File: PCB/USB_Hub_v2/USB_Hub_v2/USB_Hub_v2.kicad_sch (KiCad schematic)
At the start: 74 parts, among them J1 USB_A, J2 USB_A, J3 USB_A, J4 USB_A, J5 USB_A, J6 USB_A, SW1 SW_Push_DPDT, U1 FE1.1s, U2 TS3USB30EDGSR, U3 TPS2116DRL, U4 USBLC6-2SC6, U5 USBLC6-2SC6, U6 USBLC6-2SC6, U7 USBLC6-2SC6, U8 USBLC6-2SC6, U9 USBLC6-2SC6, Y1 12MHz

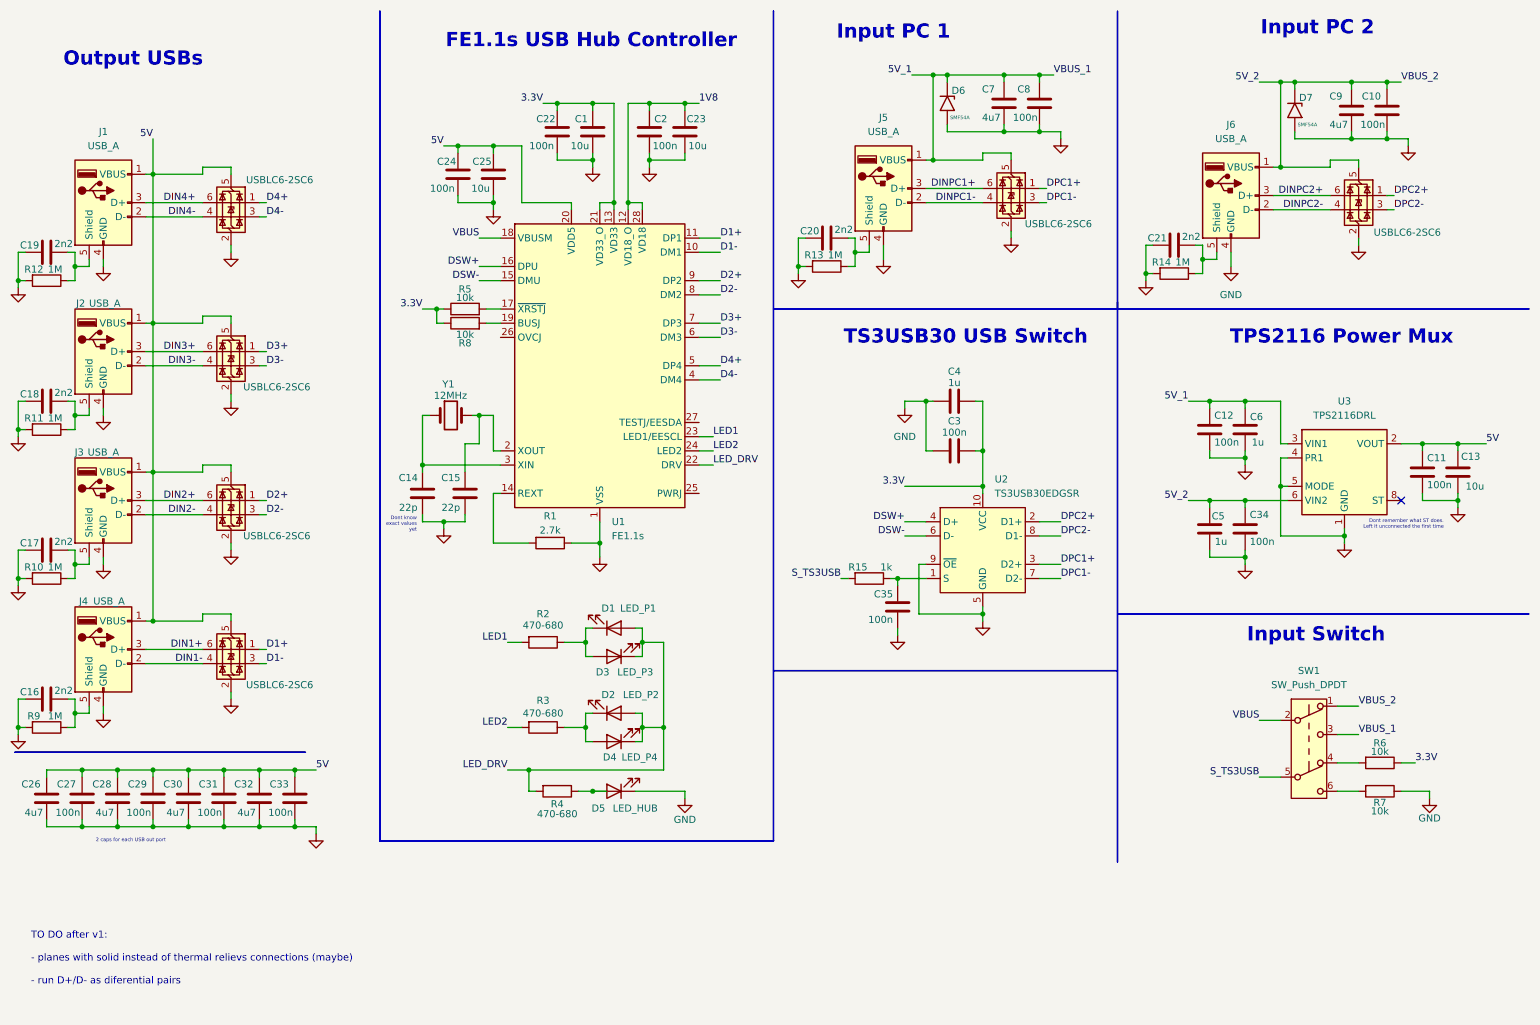
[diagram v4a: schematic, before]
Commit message: Rev 2 finished
Updated layout and added parts to improve next version
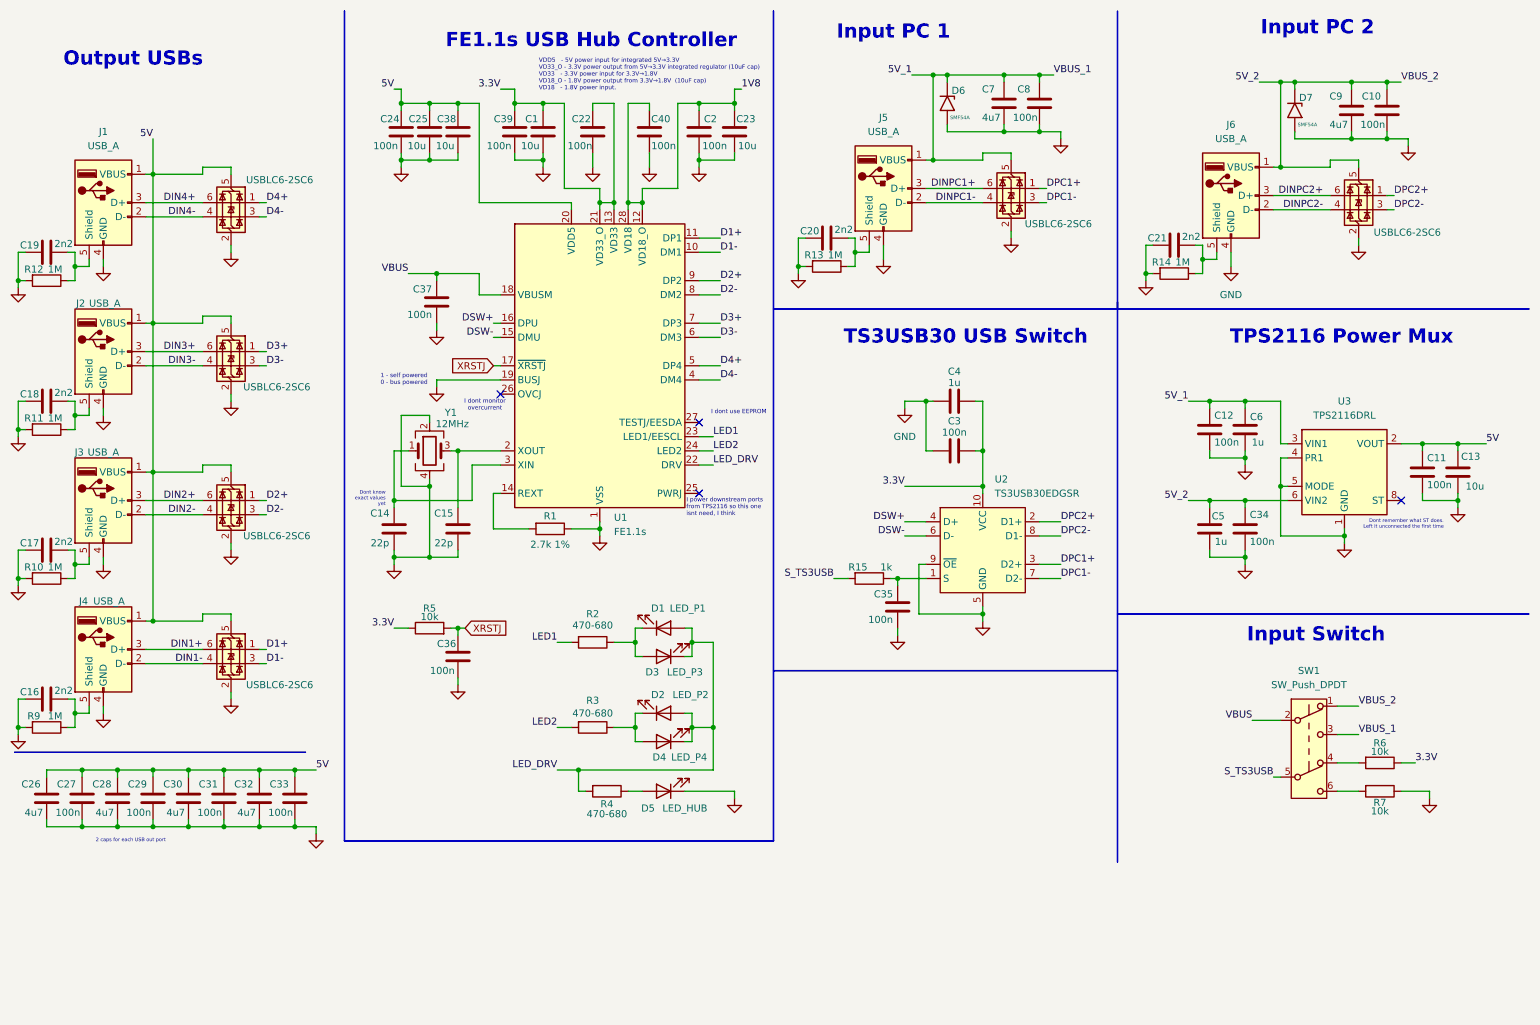
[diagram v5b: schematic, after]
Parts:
- removed R8: 10k, Resistor_SMD:R_0603_1608Metric_Pad0.98x0.95mm_HandSolder, symbol Device:R
- removed Y1: 12MHz, Crystal:Crystal_SMD_HC49-SD, symbol Device:Crystal
- added C36, C37, C39, C40: 100n, Capacitor_SMD:C_0805_2012Metric_Pad1.18x1.45mm_HandSolder, symbol Device:C
- added C38: 10u, Capacitor_SMD:C_0805_2012Metric_Pad1.18x1.45mm_HandSolder, symbol Device:C
- added Y1: 12MHz, Crystal:Crystal_SMD_3225-4Pin_3.2x2.5mm, symbol Device:Crystal_GND24
- R1: value 2.7k -> 2.7k 1%
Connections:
- net 1V8: now also C40.2
- net 3.3V: now also C39.2
- net 5V: now also C38.2
- net GND: now also U1.19 (BUSJ), C36.1, C37.1, C38.1, C39.1, C40.1, Y1.2, Y1.4
- net VBUS: now also C37.2
- net at C15.2, U1.2 (XOUT): now also Y1.3
- net XRSTJ: now reaches R5.2, U1.17 (~{XRSTJ})
- net XRSTJ: now also C36.2
- net at C14.2, U1.3 (XIN): now also Y1.1
- no-connect marks 1 -> 4
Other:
- note added: "1 - self powered 0 - bus powered"
- note added: "I dont monitor overcurrent"
- note added: "I dont use EEPROM"
- note added: "I power downstream ports from TPS2116 so this one isnt need, I think"
- note added: "VDD5 - 5V power input for integrated 5V→3.3V VD33_O - 3.3V power output from 5V→3.3V integrated regulator (10uF cap) VD33 - 3.3V power input for 3.3V→1.8V VD18_O - 1.8V power output from 3.3V→1.8V (10uF cap) VD18 - 1.8V power input."
- note removed: "TO DO after v1: - planes with solid instead of thermal relievs connections (maybe) - run D+/D- as diferential pairs"
- moved on the sheet: C1, C14, C15, C2, C22, C23, C24, C25, D1, D2, D3, D4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
